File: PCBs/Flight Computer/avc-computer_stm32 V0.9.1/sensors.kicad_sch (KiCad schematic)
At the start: 10 parts, among them U4 BNO085, U8 BMP581

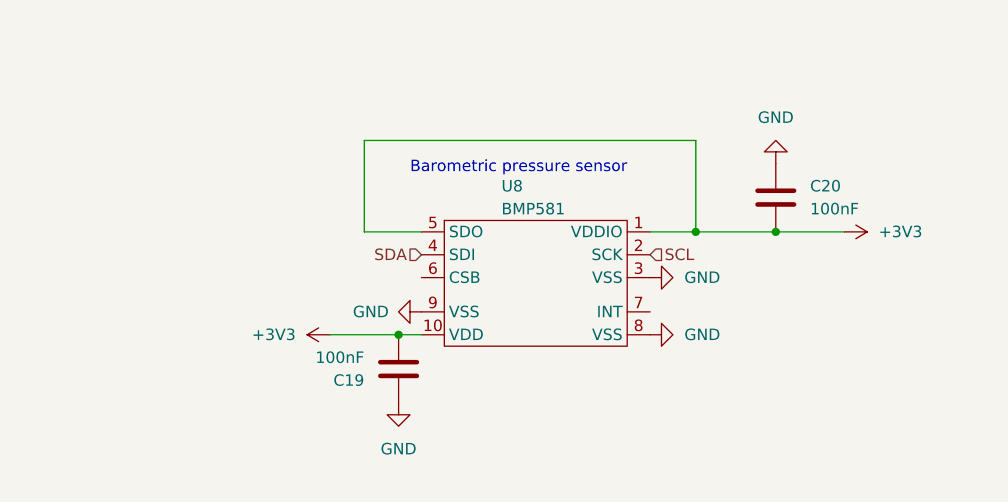
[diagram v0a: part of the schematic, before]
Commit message: Fixed all issues except for 5v buck inductor heating
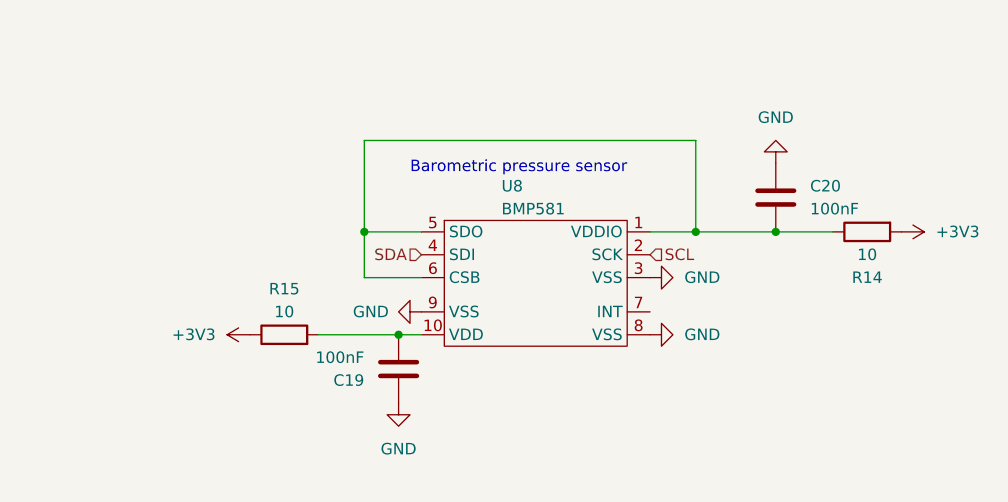
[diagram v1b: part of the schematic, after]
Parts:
- added R14, R15: 10, Resistor_SMD:R_0402_1005Metric, symbol Device:R
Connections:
- net +3V3: now also R14.2, R15.1; no longer C19.2, C20.2, U8.1 (VDDIO), U8.10 (VDD), U8.5 (SDO)
- net at U8.6 (CSB): now also C20.2, U8.1 (VDDIO), U8.5 (SDO), R14.1
- new net: C19.2, R15.2, U8.10 (VDD)
